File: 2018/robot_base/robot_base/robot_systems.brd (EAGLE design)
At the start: 100 x 80 mm, 41 parts, among them IC1 DRV8840PWP, IC2 DRV8840PWP, IC3 DRV8840PWP

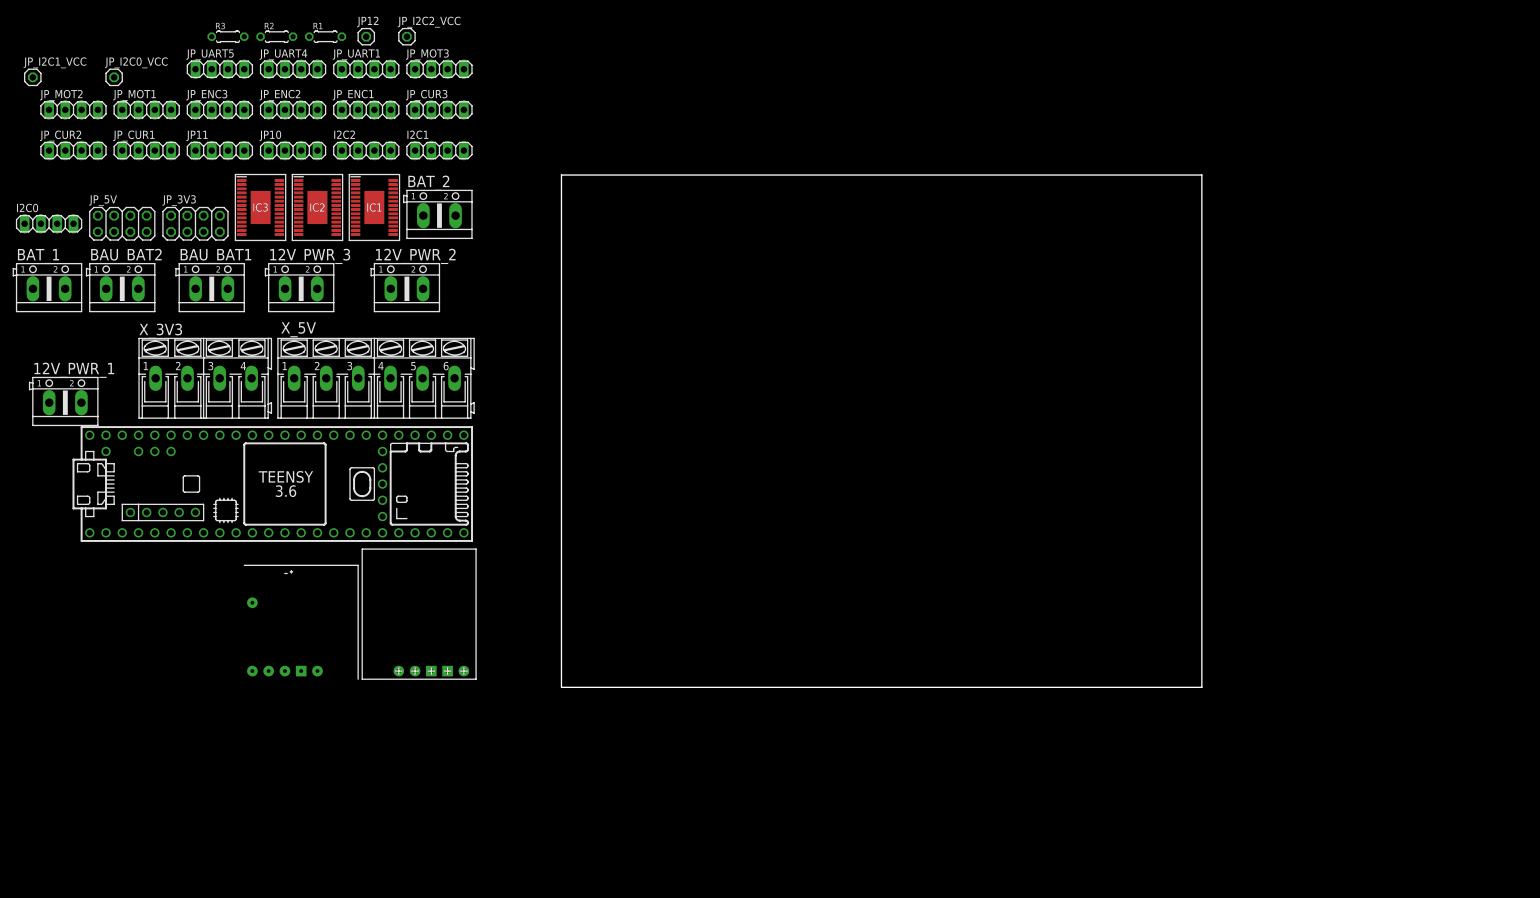
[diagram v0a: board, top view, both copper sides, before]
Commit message: Update robot_system.sch/brd: Minor corrections in sch and start to route.
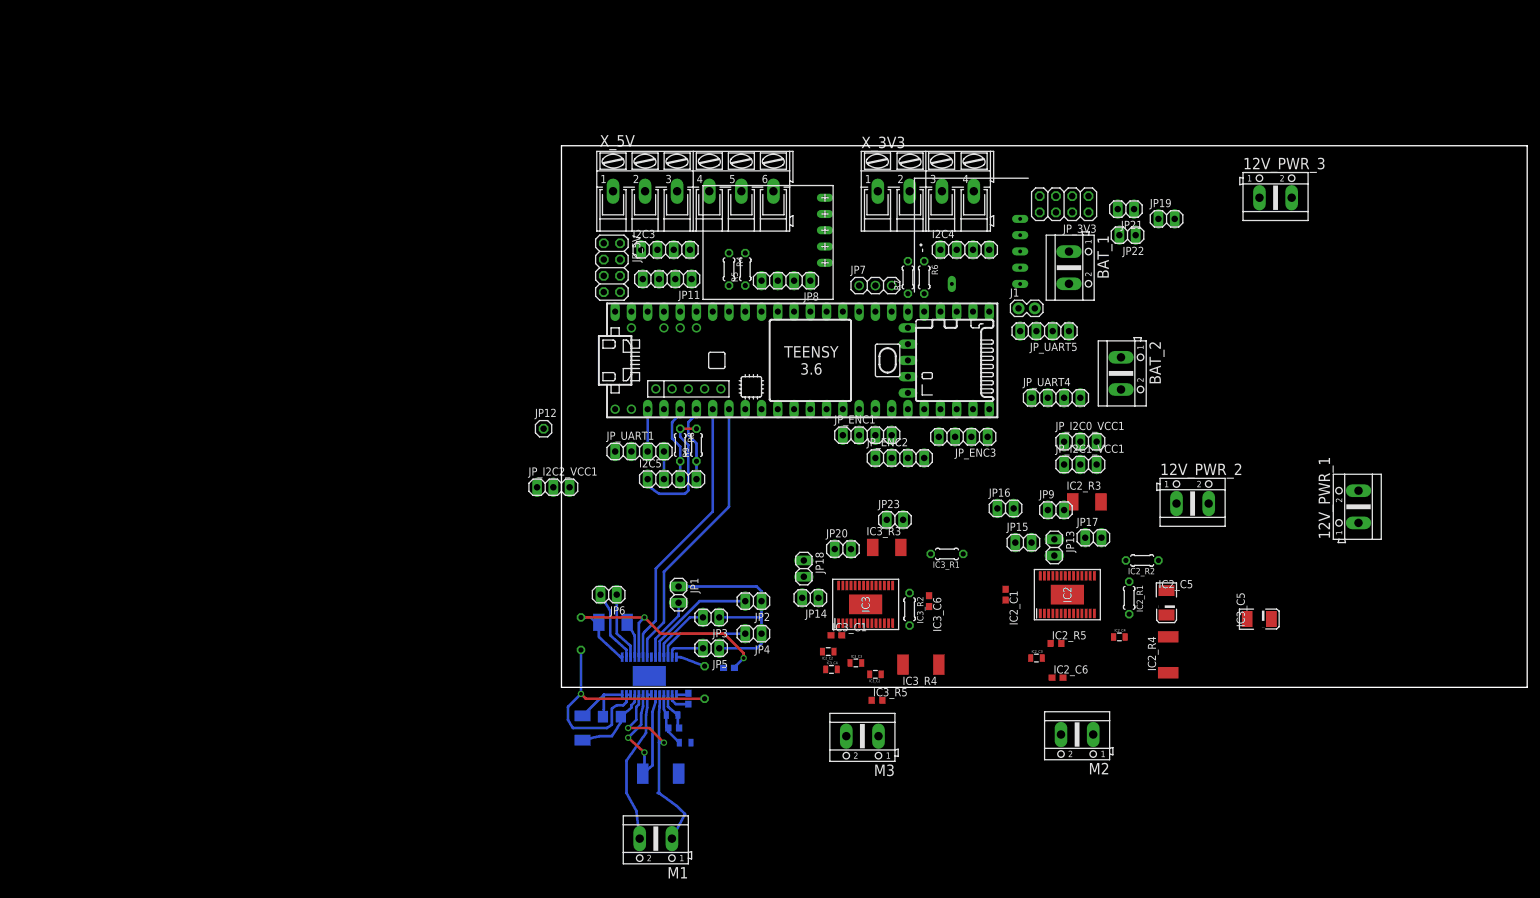
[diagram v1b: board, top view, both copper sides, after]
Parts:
- removed BAU_BAT1, BAU_BAT2: (no value), con-ptr500:AK500/2
- removed I2C0, I2C1, I2C2, JP10, JP_CUR1, JP_CUR2, JP_CUR3, JP_MOT1, JP_MOT2, JP_MOT3: (no value), pinhead:1X04
- removed JP_I2C0_VCC, JP_I2C1_VCC, JP_I2C2_VCC: (no value), pinhead:1X01
- removed R1, R2, R3: (no value), rcl:0204/5
- added I2C3, I2C4, I2C5, JP8: (no value), pinhead:1X04
- added IC1_C1, IC2_C1, IC3_C1: 0.01uF, rcl:C0603
- added IC1_C2, IC1_C3, IC2_C2, IC2_C3, IC2_C4, IC3_C2, IC3_C3, IC3_C4: 0.1uF, SparkFun-Passives:0805
- added IC1_C4: 0.1uF, SparkFun-Passives:1206
- added IC1_C5, IC2_C5, IC3_C5: 100uF, SparkFun-Passives:EIA3528-KIT
- added IC1_C6, IC2_C6, IC3_C6: 470nF, rcl:C0603
- added IC1_R1, IC1_R2, IC2_R1, IC2_R2, IC3_R1, IC3_R2: ???, resistor:0204/5
- added IC1_R3, IC2_R3, IC3_R3: 10k, rcl:R2010
- added IC1_R4, IC2_R4, IC3_R4: 100m, rcl:R2512
- added IC1_R5, IC2_R5, IC3_R5: 1M, rcl:R0603
- added J1: (no value), SparkFun-Connectors:1X02
- added JP1, JP13, JP14, JP15, JP16, JP17, JP18, JP19, JP2, JP20, JP21, JP22, JP23, JP3, JP4, JP5, JP6, JP9: (no value), pinhead:1X02
- added JP7: (no value), adafruit:1X03
- added JP_I2C0_VCC1, JP_I2C1_VCC1, JP_I2C2_VCC1: (no value), pinhead:1X03
- added M1, M2, M3: (no value), con-ptr500:AK500/2
- added R4, R5, R6, R7, R8, R9: (no value), rcl:0204/5
- U$1: value TEENSY_3.5/3.6 -> TEENSY_3.5/3.6TEENSY_3.5/3.6_LONG_PADS
- moved 12V_PWR_1 202.6 mm to (124.5, 28.2), turned to 90 degrees
- moved BAT_1 159.3 mm to (79.2, 65.5), turned to 270 degrees
- moved 12V_PWR_3 152.8 mm to (111.5, 76.5)
- moved D24V22F3 136.5 mm to (72.9, 61.7), turned to 90 degrees
- moved JP_3V3 135.7 mm to (78.5, 75.4), turned to 180 degrees
- moved JP_UART5 135.1 mm to (75.4, 55.6), turned to 180 degrees
- moved IC2 131.8 mm to (79.0, 14.5), turned to 90 degrees
- moved JP_UART4 129.7 mm to (77.2, 45.2)
- moved 12V_PWR_2 127.2 mm to (98.6, 28.7)
- moved JP_ENC3 126.8 mm to (62.7, 39.1), turned to 180 degrees
- moved X_3V3 116.5 mm to (56.9, 77.5)
- moved IC3 113.0 mm to (47.5, 13.0), turned to 90 degrees
- moved BAT_2 109.2 mm to (87.4, 49.0), turned to 270 degrees
- moved JP_ENC2 109.2 mm to (52.8, 35.8)
- moved JP_ENC1 93.3 mm to (47.8, 39.4)
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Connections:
- removed net 3V3_TEESNY_1: U$1.3V3_LO
- removed net 3V3_TEESNY_2: JP10.3, U$1.3V3
- removed net CUR3_SE: JP_CUR3.2, U$1.39/A20
- removed net MOT1_IN_A: JP_MOT1.1, U$1.8
- removed net MOT1_IN_B: JP_MOT1.2, U$1.23/A9
- removed net MOT2_IN_A: JP_MOT2.1, U$1.9/CS
- removed net MOT2_IN_B: JP_MOT2.2, U$1.22/A8
- removed net MOT3_IN_A: JP_MOT3.1, U$1.10/CS
- removed net MOT3_IN_B: JP_MOT3.2, U$1.21/A7
- removed net N$28: U$1.U5V
- removed net N$29: U$1.UD-
- removed net N$30: U$1.UD+
- removed net N$31: U$1.UGND1
- removed net N$32: U$1.UGND2
- removed net N$33: U$1.A11
- removed net N$34: U$1.A10
- removed net N$35: U$1.AREF
- removed net N$36: U$1.VUSB
- removed net N$61: U$1.RESET
- removed net N$62: U$1.PROG
- removed net N$63: U$1.GND3
- removed net N$64: U$1.3V3_2
- removed net N$65: U$1.VBAT
- new net 12V2: 12V_PWR_1.1, 12V_PWR_2.1, 12V_PWR_3.1, BAT_2.1, IC1.11, IC1.4, IC1_C2.1, IC1_C3.2, IC1_C4.2, IC1_C5.A, IC1_R5.1, IC2.11, IC2.4, IC2_C2.1, IC2_C3.2, IC2_C4.2, IC2_C5.A, IC2_R5.1, IC3.11, IC3.4, IC3_C2.1, IC3_C3.2, IC3_C4.2, IC3_C5.A, IC3_R5.1
- new net IC1_I0: IC1.23, JP1.2
- new net IC1_I1: IC1.24, JP2.2
- new net IC1_I2: IC1.25, JP3.2
- new net IC1_I3: IC1.26, JP4.2
- new net IC1_I4: IC1.27, JP5.2
- new net IC1_NFAULT: IC1.18, IC1_R3.1, U$1.2
- new net IC1_NRESET: IC1.16, JP6.2
- new net IC1_NSLEEP: IC1.17, JP6.1
- new net IC1_V3P3: IC1.15, IC1.19, IC1_C6.1, IC1_R1.1, IC1_R3.2
- new net IC2_I0: IC2.23, JP9.2
- new net IC2_I1: IC2.24, JP13.2
- new net IC2_I2: IC2.25, JP14.2
- new net IC2_I3: IC2.26, JP15.2
- new net IC2_I4: IC2.27, JP16.2
- new net IC2_NFAULT: IC2.18, IC2_R3.1, U$1.7
- new net IC2_NRESET: IC2.16, JP17.2
- new net IC2_NSLEEP: IC2.17, JP17.1
- new net IC2_V3P3: IC2.15, IC2.19, IC2_C6.1, IC2_R1.1, IC2_R3.2
- new net IC3_I0: IC3.23, JP18.2
- new net IC3_I1: IC3.24, JP19.2
- new net IC3_I2: IC3.25, JP20.2
- new net IC3_I3: IC3.26, JP21.2
- new net IC3_I4: IC3.27, JP22.2
- new net IC3_NFAULT: IC3.18, IC3_R3.1, U$1.10/CS
- new net IC3_NRESET: IC3.16, JP23.2
- new net IC3_NSLEEP: IC3.17, JP23.1
- new net IC3_R2: IC3.12, IC3.13, IC3_R1.2, IC3_R2.2
- new net IC3_V3P3: IC3.15, IC3.19, IC3_C6.1, IC3_R1.1, IC3_R3.2
- new net M1_1: IC1.10, IC1.5, M1.1
- new net M1_2: IC1.7, IC1.8, M1.2
- new net M2_1: IC2.10, IC2.5, M2.1
- new net M2_2: IC2.7, IC2.8, M2.2
- new net M3_1: IC3.10, IC3.5, M3.1
- new net M3_2: IC3.7, IC3.8, M3.2
- new net MOT1_DIR: IC1.20, U$1.5
- new net MOT2_DIR: IC2.20, U$1.8
- new net MOT3_DIR: IC3.20, U$1.29
- new net N$12: IC1.3, IC1_C2.2, IC1_R5.2
- new net N$13: IC2.1, IC2_C1.1
- new net N$14: IC2.2, IC2_C1.2
- new net N$15: IC2.3, IC2_C2.2, IC2_R5.2
- new net N$17: IC3.6, IC3.9, IC3_R4.2
- new net N$18: IC3.1, IC3_C1.1
- new net N$19: IC3.2, IC3_C1.2
- new net N$20: IC3.3, IC3_C2.2, IC3_R5.2
- new net NS50: JP7.3, U$1.39/A20
- net 3V3: now also JP1.1, JP13.1, JP14.1, JP15.1, JP16.1, JP18.1, JP19.1, JP2.1, JP20.1, JP21.1, JP22.1, JP3.1, JP4.1, JP5.1, JP9.1, JP_I2C0_VCC1.3, JP_I2C1_VCC1.3, JP_I2C2_VCC1.3
- net 5V: now also JP_I2C0_VCC1.1, JP_I2C1_VCC1.1, JP_I2C2_VCC1.1; no longer JP_CUR1.3, JP_CUR2.3, JP_CUR3.3
- net CUR1_NF: now also JP11.1; no longer JP_CUR1.1
- net CUR1_SE: now also JP8.4; no longer JP_CUR1.2
- net CUR2_NF: now also JP8.3; no longer JP_CUR2.1
- net CUR2_SE: now also JP8.2; no longer JP_CUR2.2
- net CUR3_NF: now also JP8.1; no longer JP_CUR3.1
- net ENC1_A: now also U$1.12/MISO; no longer U$1.25
- net ENC1_B: now also U$1.24; no longer U$1.26
- net ENC2_A: now also U$1.25; no longer U$1.27
- net ENC2_B: now also U$1.26; no longer U$1.28
- net ENC3_A: now also U$1.27; no longer U$1.29
- net ENC3_B: now also U$1.28; no longer U$1.30
- net GND: now also I2C3.2, I2C4.2, I2C5.2, IC1.14, IC1.28, IC1.29, IC1_C3.1, IC1_C4.1, IC1_C5.C, IC1_C6.2, IC1_R2.1, IC1_R4.1, IC2.14, IC2.28, IC2.29, IC2_C3.1, IC2_C4.1, IC2_C5.C, IC2_C6.2, IC2_R2.1, IC2_R4.1, IC3.14, IC3.28, IC3.29, IC3_C3.1, IC3_C4.1, IC3_C5.C, IC3_C6.2, IC3_R2.1, IC3_R4.1; no longer I2C0.2, I2C1.2, I2C2.2, JP_CUR1.4, JP_CUR2.4, JP_CUR3.4, JP_MOT1.4, JP_MOT2.4, JP_MOT3.4
- net I2C0_VCC: now also I2C3.1, JP_I2C0_VCC1.2, R4.1, R5.2; no longer I2C0.1, R1.1
- net I2C1_VCC: now also I2C4.1, JP_I2C1_VCC1.2, R6.1, R7.2; no longer I2C1.1, R2.1
- net I2C2_VCC: now also I2C5.1, JP_I2C2_VCC1.2, R8.1, R9.2; no longer I2C2.1, R3.1
- net MOT1_PWM: now also IC1.21, U$1.6; no longer JP_MOT1.3, U$1.5
- net MOT2_PWM: now also IC2.21, U$1.9/CS; no longer JP_MOT2.3, U$1.6
- net MOT3_PWM: now also IC3.21, U$1.30; no longer JP_MOT3.3, U$1.7
- net N$1: now also JP11.4, U$1.23/A9; no longer JP10.1, U$1.11/MOSI
- net N$10: now also IC1.1, IC1_C1.1; no longer JP_I2C1_VCC.1, R2.2
- net N$11: now also IC1.2, IC1_C1.2; no longer JP_I2C2_VCC.1, R3.2
- net N$2: now also IC1.12, IC1.13, IC1_R1.2, IC1_R2.2; no longer 12V_PWR_1.1, 12V_PWR_2.1, 12V_PWR_3.1, BAU_BAT2.2
- net N$3: now also IC2.12, IC2.13, IC2_R1.2, IC2_R2.2; no longer BAT_2.1, BAU_BAT2.1
- net N$4: now also JP11.3, U$1.22/A8; no longer JP10.2, U$1.12/MISO
- net N$5: now also IC1.6, IC1.9, IC1_R4.2; no longer BAU_BAT1.1, D24V22F3.VIN, D24V50F5.VIN
- net N$52: now also JP7.1; no longer JP11.4
- net N$53: now also JP7.2; no longer JP11.3
- net N$57: now also J1.1; no longer JP11.2
- net N$58: now also J1.2; no longer JP11.1
- net N$6: now also JP11.2, U$1.21/A7; no longer JP10.4, U$1.24
- net N$7: now also U$1.11/MOSI; no longer U$1.2
- net N$8: now also D24V22F3.VIN, D24V50F5.VIN; no longer BAU_BAT1.2
- net N$9: now also IC2.6, IC2.9, IC2_R4.2; no longer JP_I2C0_VCC.1, R1.2
- net SCL0: now also I2C3.3, R4.2; no longer I2C0.3
- net SCL1: now also I2C4.3, R6.2; no longer I2C1.3
- net SCL2: now also I2C5.3, R8.2; no longer I2C2.3
- net SDA0: now also I2C3.4, R5.1; no longer I2C0.4
- net SDA1: now also I2C4.4, R7.1; no longer I2C1.4
- net SDA2: now also I2C5.4, R9.1; no longer I2C2.4
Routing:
- net IC1_V3P3: track 0.00 -> 47.7 mm, vias 0 -> 2
- net N$2: track 0.00 -> 46.1 mm, vias 0 -> 1
- net MOT1_PWM: track 0.00 -> 44.0 mm
- net MOT1_DIR: track 0.00 -> 43.2 mm
- net M1_1: track 0.00 -> 38.4 mm, vias 0 -> 2
- net 3V3: track 0.00 -> 35.0 mm
- net N$5: track 0.00 -> 27.5 mm, vias 0 -> 2
- net M1_2: track 0.00 -> 24.5 mm
- net 12V2: track 0.00 -> 20.9 mm
- net I2C2_VCC: track 0.00 -> 20.7 mm
- net GND: track 0.00 -> 20.0 mm
- net IC1_I1: track 0.00 -> 18.4 mm
- net IC1_I3: track 0.00 -> 14.6 mm
- net SCL2: track 0.00 -> 12.0 mm
- net SDA2: track 0.00 -> 12.0 mm
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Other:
- board size 100 x 80 mm -> 150.8 x 84.6 mm

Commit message: Update and complete routing of robot_system board. Last checks TODO.
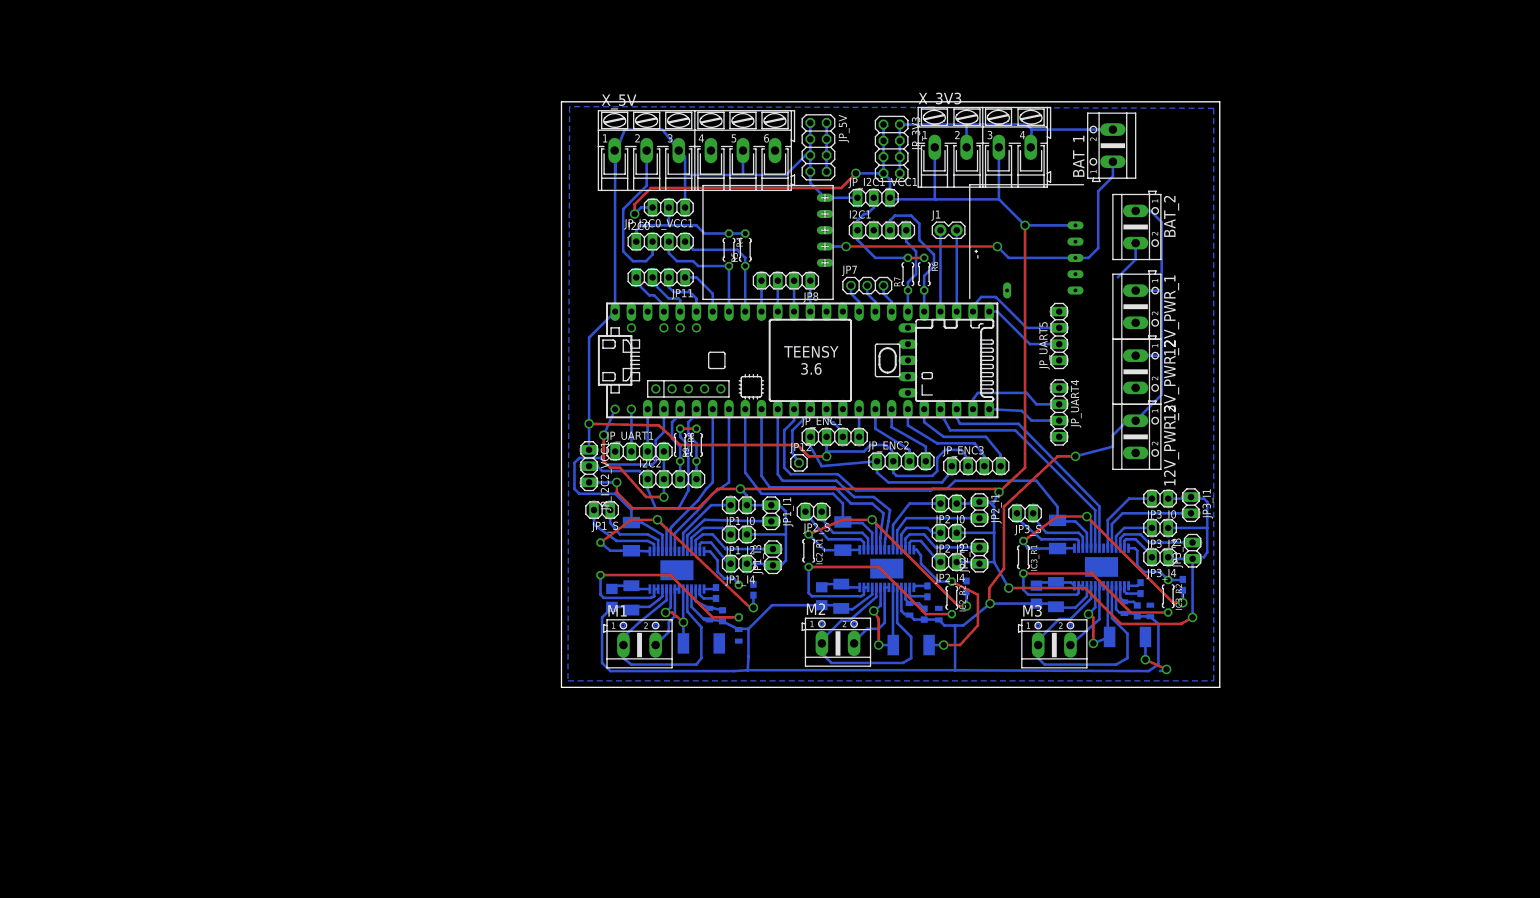
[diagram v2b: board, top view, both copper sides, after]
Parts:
- removed I2C3, I2C4: (no value), pinhead:1X04
- removed JP1, JP13, JP14, JP15, JP16, JP17, JP18, JP19, JP2, JP20, JP21, JP22, JP23, JP3, JP4, JP5, JP6, JP9: (no value), pinhead:1X02
- added I2C0, I2C1: (no value), pinhead:1X04
- added JP1_I0, JP1_I1, JP1_I2, JP1_I3, JP1_I4, JP1_S, JP2_I0, JP2_I1, JP2_I2, JP2_I3, JP2_I4, JP2_S, JP3_I0, JP3_I1, JP3_I2, JP3_I3, JP3_I4, JP3_S: (no value), pinhead:1X02
- IC2_C4, IC3_C4: device SparkFun-Passives:0805 -> SparkFun-Passives:1206
- moved JP_I2C0_VCC1 73.9 mm to (16.8, 74.9), turned to 180 degrees
- moved JP_I2C1_VCC1 52.7 mm to (48.8, 76.5)
- moved IC2_C5 50.8 mm to (43.7, 14.2), flipped to the bottom
- moved IC2_R1 50.6 mm to (38.6, 21.3)
- moved IC3_C1 48.1 mm to (90.4, 15.5), flipped to the bottom, turned to 270 degrees
- moved IC2_C4 46.9 mm to (40.6, 14.2), flipped to the bottom, turned to 270 degrees
- moved 12V_PWR_1 46.8 mm to (89.7, 59.4), turned to 270 degrees
- moved IC3_C3 46.7 mm to (91.9, 11.9), flipped to the bottom, turned to 270 degrees
- moved 12V_PWR_3 43.3 mm to (89.7, 39.1), turned to 270 degrees
- moved IC3_R5 43.0 mm to (89.9, 11.9), flipped to the bottom, turned to 90 degrees
- moved IC3_R2 40.4 mm to (94.7, 14.2)
- moved IC3_C2 40.2 mm to (87.9, 12.4), flipped to the bottom, turned to 90 degrees
- moved JP12 40.2 mm to (37.1, 35.1)
- moved IC2_R4 40.2 mm to (54.6, 6.60), flipped to the bottom, turned to 0 degrees
- moved M2 40.0 mm to (43.2, 6.86), turned to 0 degrees
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- renumbered I2C5 to I2C2
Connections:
- net 3V3: now also JP1_I0.1, JP1_I1.1, JP1_I2.1, JP1_I3.1, JP1_I4.1, JP2_I0.1, JP2_I1.1, JP2_I2.1, JP2_I3.1, JP2_I4.1, JP3_I0.1, JP3_I1.1, JP3_I2.1, JP3_I3.1, JP3_I4.1; no longer JP1.1, JP13.1, JP14.1, JP15.1, JP16.1, JP18.1, JP19.1, JP2.1, JP20.1, JP21.1, JP22.1, JP3.1, JP4.1, JP5.1, JP9.1
- net GND: now also I2C0.2, I2C1.2; no longer I2C3.2, I2C4.2
- net I2C0_VCC: now also I2C0.1; no longer I2C3.1
- net I2C1_VCC: now also I2C1.1; no longer I2C4.1
- net IC1_I0: now also JP1_I0.2; no longer JP1.2
- net IC1_I1: now also JP1_I1.2; no longer JP2.2
- net IC1_I2: now also JP1_I2.2; no longer JP3.2
- net IC1_I3: now also JP1_I3.2; no longer JP4.2
- net IC1_I4: now also JP1_I4.2; no longer JP5.2
- net IC1_NRESET: now also JP1_S.2; no longer JP6.2
- net IC1_NSLEEP: now also JP1_S.1; no longer JP6.1
- net IC2_I0: now also JP2_I0.2; no longer JP9.2
- net IC2_I1: now also JP2_I1.2; no longer JP13.2
- net IC2_I2: now also JP2_I2.2; no longer JP14.2
- net IC2_I3: now also JP2_I3.2; no longer JP15.2
- net IC2_I4: now also JP2_I4.2; no longer JP16.2
- net IC2_NRESET: now also JP2_S.2; no longer JP17.2
- net IC2_NSLEEP: now also JP2_S.1; no longer JP17.1
- net IC3_I0: now also JP3_I0.2; no longer JP18.2
- net IC3_I1: now also JP3_I1.2; no longer JP19.2
- net IC3_I2: now also JP3_I2.2; no longer JP20.2
- net IC3_I3: now also JP3_I3.2; no longer JP21.2
- net IC3_I4: now also JP3_I4.2; no longer JP22.2
- net IC3_NRESET: now also JP3_S.2; no longer JP23.2
- net IC3_NSLEEP: now also JP3_S.1; no longer JP23.1
- net SCL0: now also I2C0.3; no longer I2C3.3
- net SCL1: now also I2C1.3; no longer I2C4.3
- net SDA0: now also I2C0.4; no longer I2C3.4
- net SDA1: now also I2C1.4; no longer I2C4.4
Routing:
- net 3V3: track 35.0 -> 347.1 mm, vias 0 -> 8
- net 12V2: track 20.9 -> 301.8 mm, vias 0 -> 2
- net GND: track 20.0 -> 218.7 mm, vias 0 -> 5
- net 5V: track 0.00 -> 191.0 mm, vias 0 -> 2
- net IC3_NFAULT: track 0.00 -> 66.3 mm
- net N$8: track 0.00 -> 58.5 mm, vias 0 -> 2
- net IC3_V3P3: track 0.00 -> 47.5 mm, vias 0 -> 2
- net IC2_V3P3: track 0.00 -> 46.8 mm, vias 0 -> 2
- net M3_1: track 0.00 -> 42.7 mm
- net M2_1: track 0.00 -> 41.7 mm
- net IC1_NFAULT: track 5.76 -> 46.5 mm
- net N$3: track 0.00 -> 40.1 mm
- net IC3_R2: track 0.00 -> 38.5 mm
- net IC2_NFAULT: track 0.00 -> 38.2 mm
- net MOT2_DIR: track 0.00 -> 37.7 mm
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- added copper zone on layer 16, net GND
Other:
- board size 150.8 x 84.6 mm -> 102.8 x 91.4 mm
